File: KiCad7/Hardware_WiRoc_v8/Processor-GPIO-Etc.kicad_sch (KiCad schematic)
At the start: 6 parts

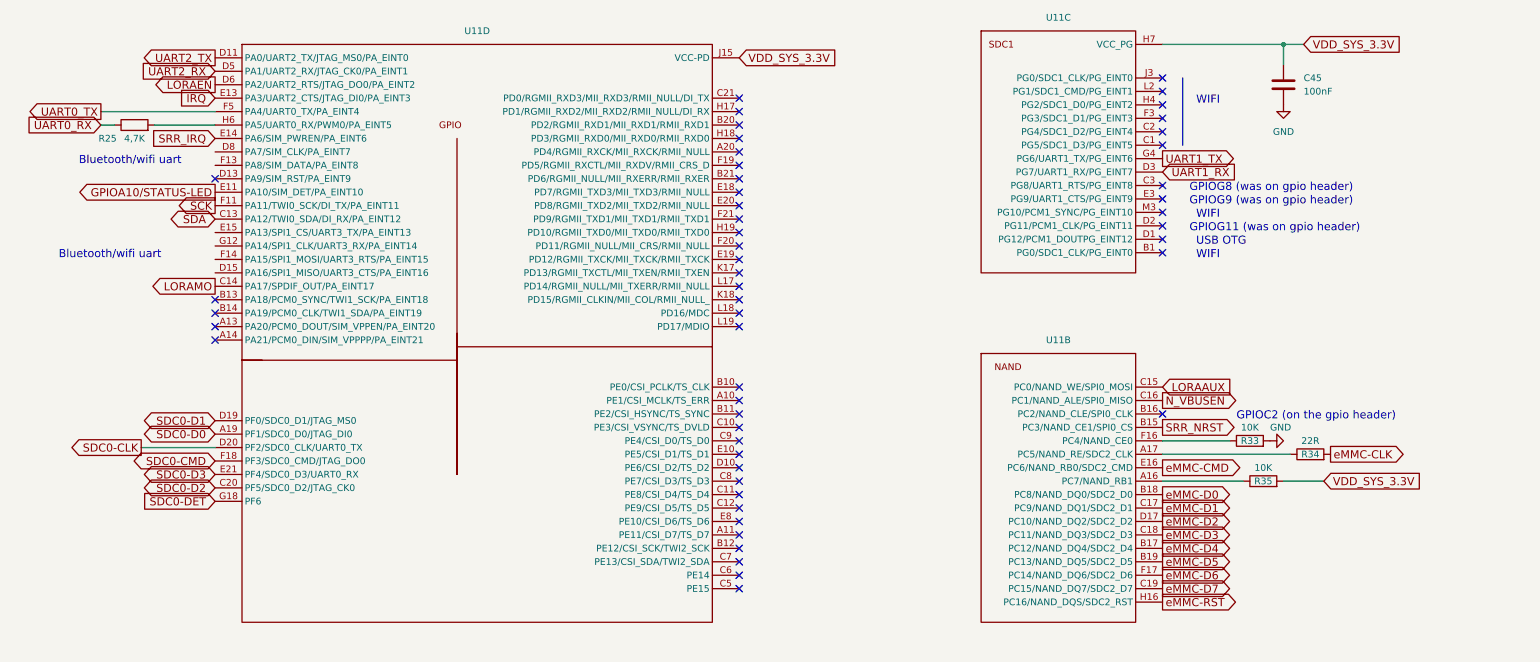
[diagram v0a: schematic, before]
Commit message: wiroc v8 layout work
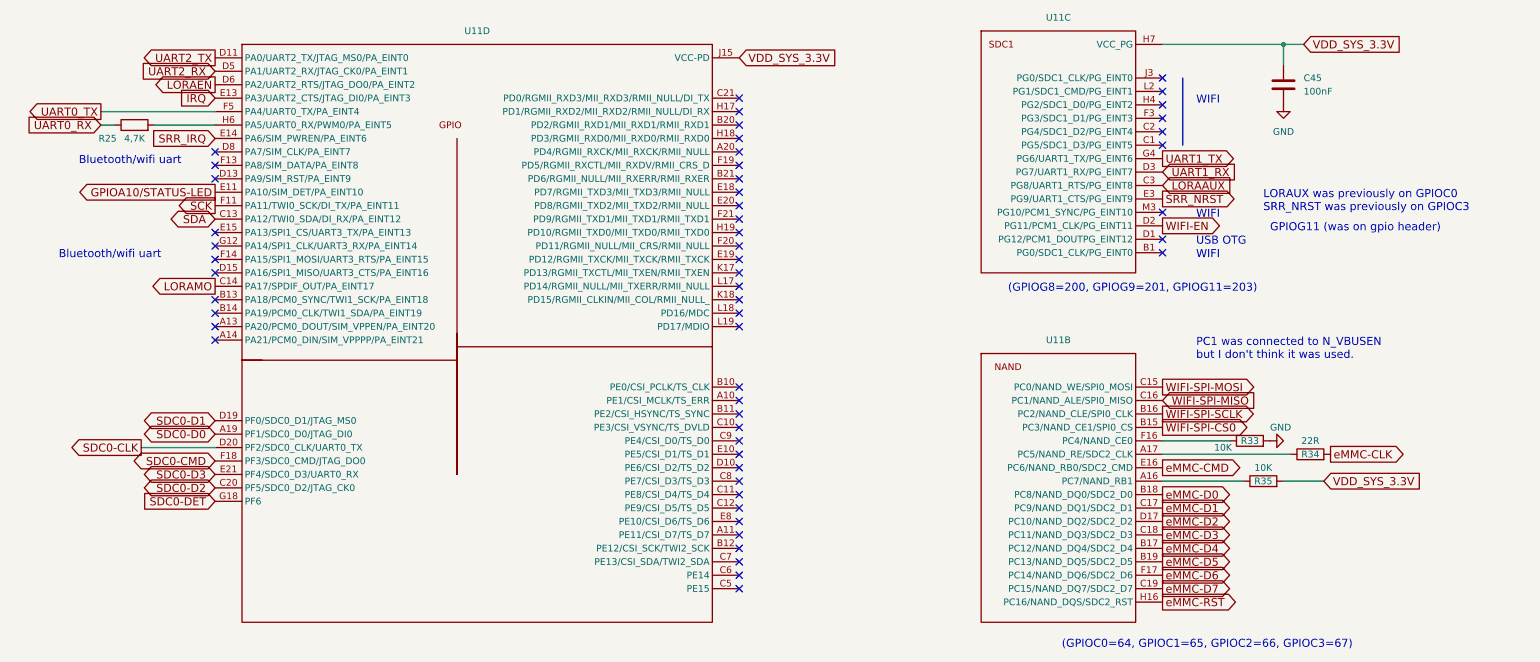
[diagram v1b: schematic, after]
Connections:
- net LORAAUX: now also U11.C3 (PG8/UART1_RTS/PG_EINT8); no longer U11.C15 (PC0/NAND_WE/SPI0_MOSI)
- net SRR_NRST: now also U11.E3 (PG9/UART1_CTS/PG_EINT9); no longer U11.B15 (PC3/NAND_CE1/SPI0_CS)
- net WIFI-SPI-SCLK: now reaches U11.B16 (PC2/NAND_CLE/SPI0_CLK)
- net WIFI-EN: now reaches U11.D2 (PG11/PCM1_CLK/PG_EINT11)
- net N_VBUSEN renamed WIFI-SPI-MISO
- new net WIFI-SPI-CS0: U11.B15 (PC3/NAND_CE1/SPI0_CS)
- new net WIFI-SPI-MOSI: U11.C15 (PC0/NAND_WE/SPI0_MOSI)
- no-connect marks 52 -> 54
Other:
- note added: "(GPIOC0=64, GPIOC1=65, GPIOC2=66, GPIOC3=67)"
- note added: "(GPIOG8=200, GPIOG9=201, GPIOG11=203)"
- note added: "LORAUX was previously on GPIOC0 SRR_NRST was previously on GPIOC3"
- note added: "PC1 was connected to N_VBUSEN but I don't think it was used."
- note removed: "GPIOC2 (on the gpio header)"
- note removed: "GPIOG8 (was on gpio header)"
- note removed: "GPIOG9 (was on gpio header)"
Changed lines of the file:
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@@
   (no_connect (at 234.95 45.72))
   (no_connect (at 154.94 54.61))
+  (no_connect (at 55.88 59.69))
   (no_connect (at 154.94 87.63))
   (no_connect (at 234.95 58.42))
   (no_connect (at 154.94 72.39))
-  (no_connect (at 234.95 66.04))
   (no_connect (at 154.94 69.85))
   (no_connect (at 154.94 92.71))
+  (no_connect (at 55.88 82.55))
   (no_connect (at 154.94 80.01))
   (no_connect (at 154.94 121.92))
@@
   (no_connect (at 154.94 109.22))
   (no_connect (at 154.94 67.31))
+  (no_connect (at 55.88 62.23))
+  (no_connect (at 55.88 80.01))
   (no_connect (at 154.94 119.38))
   (no_connect (at 154.94 62.23))
-  (no_connect (at 234.95 73.66))
   (no_connect (at 55.88 95.25))
   (no_connect (at 55.88 64.77))
@@
   (no_connect (at 154.94 85.09))
   (no_connect (at 154.94 57.15))
+  (no_connect (at 55.88 77.47))
   (no_connect (at 154.94 64.77))
   (no_connect (at 234.95 53.34))
@@
   (no_connect (at 154.94 139.7))
   (no_connect (at 234.95 48.26))
-  (no_connect (at 234.95 68.58))
   (no_connect (at 154.94 142.24))
   (no_connect (at 154.94 104.14))
@@
   (no_connect (at 55.88 92.71))
   (no_connect (at 234.95 78.74))
+  (no_connect (at 55.88 74.93))
   (no_connect (at 154.94 49.53))
-  (no_connect (at 234.95 109.22))
   (no_connect (at 154.94 137.16))
   (no_connect (at 234.95 55.88))
@@
     (effects (font (size 1.524 1.524)) (justify left bottom))
   )
+  (text "(GPIOG8=200, GPIOG9=201, GPIOG11=203)" (at 205.74 86.36 0)
+    (effects (font (size 1.524 1.524)) (justify left bottom))
+  )
   (text "USB OTG" (at 241.3 77.47 0)
     (effects (font (size 1.524 1.524)) (justify left bottom))
   )
-  (text "GPIOC2 (on the gpio header)" (at 248.92 110.49 0)
+  (text "PC1 was connected to N_VBUSEN\nbut I don't think it was used."
+    (at 241.3 99.06 0)
     (effects (font (size 1.524 1.524)) (justify left bottom))
   )
-  (text "GPIOG8 (was on gpio header)" (at 240.03 67.31 0)
-    (effects (font (size 1.524 1.524)) (justify left bottom))
-  )
-  (text "GPIOG11 (was on gpio header)" (at 240.03 74.93 0)
+  (text "GPIOG11 (was on gpio header)" (at 255.27 74.93 0)
     (effects (font (size 1.524 1.524)) (justify left bottom))
   )
@@
     (effects (font (size 1.524 1.524)) (justify right bottom))
   )
-  (text "GPIOG9 (was on gpio header)" (at 240.03 69.85 0)
+  (text "LORAUX was previously on GPIOC0\nSRR_NRST was previously on GPIOC3"
+    (at 254 71.12 0)
+    (effects (font (size 1.524 1.524)) (justify left bottom))
+  )
+  (text "(GPIOC0=64, GPIOC1=65, GPIOC2=66, GPIOC3=67)" (at 215.9 153.67 0)
     (effects (font (size 1.524 1.524)) (justify left bottom))
   )
@@
     )
   )
-  (global_label "LORAAUX" (shape input) (at 234.95 104.14 0) (fields_autoplaced)
-    (effects (font (size 1.524 1.524)) (justify left))
-    (property "Intersheetrefs" "${INTERSHEET_REFS}" (at 247.7617 104.14 0)
+  (global_label "LORAAUX" (shape input) (at 234.95 66.04 0) (fields_autoplaced)
+    (effects (font (size 1.524 1.524)) (justify left))
+    (property "Intersheetrefs" "${INTERSHEET_REFS}" (at 247.7617 66.04 0)
       (effects (font (size 1.27 1.27)) (justify left) hide)
     )
   )
-  (global_label "SRR_NRST" (shape output) (at 234.95 111.76 0) (fields_autoplaced)
-    (effects (font (size 1.524 1.524)) (justify left))
-    (property "Intersheetrefs" "${INTERSHEET_REFS}" (at 249.1326 111.6648 0)
+  (global_label "SRR_NRST" (shape output) (at 234.95 68.58 0) (fields_autoplaced)
+    (effects (font (size 1.524 1.524)) (justify left))
+    (property "Intersheetrefs" "${INTERSHEET_REFS}" (at 249.1326 68.4848 0)
       (effects (font (size 1.524 1.524)) (justify left) hide)
     )
@@
     (property "Intersheetrefs" "${INTERSHEET_REFS}" (at 41.1271 120.65 0)
       (effects (font (size 1.27 1.27)) (justify right) hide)
-    )
-  )
-  (global_label "N_VBUSEN" (shape output) (at 234.95 106.68 0) (fields_autoplaced)
-    (effects (font (size 1.524 1.524)) (justify left))
-    (property "Intersheetrefs" "${INTERSHEET_REFS}" (at 249.3583 106.68 0)
-      (effects (font (size 1.27 1.27)) (justify left) hide)
     )
   )
@@
     )
   )
+  (global_label "WIFI-SPI-MOSI" (shape output) (at 234.95 104.14 0) (fields_autoplaced)
+    (effects (font (size 1.524 1.524)) (justify left))
+    (property "Intersheetrefs" "${INTERSHEET_REFS}" (at 255.2365 104.14 0)
+      (effects (font (size 1.27 1.27)) (justify left) hide)
+    )
+  )
   (global_label "eMMC-RST" (shape output) (at 234.95 144.78 0) (fields_autoplaced)
     (effects (font (size 1.524 1.524)) (justify left))
@@
     )
   )
+  (global_label "WIFI-SPI-MISO" (shape input) (at 234.95 106.68 0) (fields_autoplaced)
+    (effects (font (size 1.524 1.524)) (justify left))
+    (property "Intersheetrefs" "${INTERSHEET_REFS}" (at 255.2365 106.68 0)
+      (effects (font (size 1.27 1.27)) (justify left) hide)
+    )
+  )
   (global_label "eMMC-CLK" (shape output) (at 266.7 116.84 0) (fields_autoplaced)
     (effects (font (size 1.524 1.524)) (justify left))
@@
     )
   )
+  (global_label "WIFI-SPI-CS0" (shape output) (at 234.95 111.76 0) (fields_autoplaced)
+    (effects (font (size 1.524 1.524)) (justify left))
+    (property "Intersheetrefs" "${INTERSHEET_REFS}" (at 254.1479 111.76 0)
+      (effects (font (size 1.27 1.27)) (justify left) hide)
+    )
+  )
+  (global_label "WIFI-SPI-SCLK" (shape output) (at 234.95 109.22 0) (fields_autoplaced)
+    (effects (font (size 1.524 1.524)) (justify left))
+    (property "Intersheetrefs" "${INTERSHEET_REFS}" (at 255.4542 109.22 0)
+      (effects (font (size 1.27 1.27)) (justify left) hide)
+    )
+  )
   (global_label "UART1_RX" (shape input) (at 234.95 63.5 0) (fields_autoplaced)
     (effects (font (size 1.524 1.524)) (justify left))
     (property "Intersheetrefs" "${INTERSHEET_REFS}" (at 248.8273 63.5 0)
+      (effects (font (size 1.27 1.27)) (justify left) hide)
+    )
+  )
+  (global_label "WIFI-EN" (shape output) (at 234.95 73.66 0) (fields_autoplaced)
+    (effects (font (size 1.524 1.524)) (justify left))
+    (property "Intersheetrefs" "${INTERSHEET_REFS}" (at 247.1086 73.66 0)
       (effects (font (size 1.27 1.27)) (justify left) hide)
     )
@@
       (effects (font (size 1.27 1.27)))
     )
-    (property "Value" "10K" (at 251.46 111.76 90)
+    (property "Value" "10K" (at 246.38 115.57 90)
       (effects (font (size 1.27 1.27)))
     )

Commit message: more routing of v8
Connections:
- net WIFI-DataReady: now reaches U11.L18 (PD16/MDC)
- net WIFI-HandShake: now reaches U11.L19 (PD17/MDIO)
- no-connect marks 54 -> 52
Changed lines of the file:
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@@
   (no_connect (at 154.94 72.39))
   (no_connect (at 154.94 69.85))
-  (no_connect (at 154.94 92.71))
   (no_connect (at 55.88 82.55))
   (no_connect (at 154.94 80.01))
@@
   (no_connect (at 55.88 90.17))
   (no_connect (at 234.95 71.12))
-  (no_connect (at 154.94 90.17))
   (no_connect (at 154.94 139.7))
   (no_connect (at 234.95 48.26))
@@
     (stroke (width 0) (type default))
   )
+  (wire (pts (xy 154.94 92.71) (xy 162.56 92.71))
+    (stroke (width 0) (type default))
+  )
   (wire (pts (xy 234.95 121.92) (xy 250.19 121.92))
     (stroke (width 0) (type default))
@@
   )
   (wire (pts (xy 41.91 115.57) (xy 55.88 115.57))
+    (stroke (width 0) (type default))
+  )
+  (wire (pts (xy 154.94 90.17) (xy 162.56 90.17))
     (stroke (width 0) (type default))
   )
@@
     )
   )
+  (global_label "WIFI-HandShake" (shape input) (at 162.56 92.71 0) (fields_autoplaced)
+    (effects (font (size 1.524 1.524)) (justify left))
+    (property "Intersheetrefs" "${INTERSHEET_REFS}" (at 184.2256 92.71 0)
+      (effects (font (size 1.27 1.27)) (justify left) hide)
+    )
+  )
   (global_label "SDC0-D3" (shape bidirectional) (at 55.88 120.65 180) (fields_autoplaced)
     (effects (font (size 1.524 1.524)) (justify right))
@@
     )
   )
+  (global_label "WIFI-DataReady" (shape input) (at 162.56 90.17 0) (fields_autoplaced)
+    (effects (font (size 1.524 1.524)) (justify left))
+    (property "Intersheetrefs" "${INTERSHEET_REFS}" (at 183.645 90.17 0)
+      (effects (font (size 1.27 1.27)) (justify left) hide)
+    )
+  )
